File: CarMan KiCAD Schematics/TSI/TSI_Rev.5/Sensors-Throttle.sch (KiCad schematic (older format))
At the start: 55 parts, among them J24 MC+ Short Pin 1, J25 MC+ Short Pin 2, J26 HV+ Short Pin 1, J27 HV+ Short Pin 2, J28 HV- Short Pin 1, J29 HV- Short Pin 2, U21 MCP6004, U25 NCD9830DBR2G, U26 MCP6004, U4 ACPL-C870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

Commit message: Small Changes & Updated PCB
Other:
- moved on the sheet: R104
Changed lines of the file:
@@
 Wire Wire Line
 	11800 5700 11800 5900
-Text Label 10400 5750 0    50   ~ 0
-DiffAmp_REF
-Wire Wire Line
-	10400 5750 10400 5800
 Wire Wire Line
 	10400 6200 10550 6200
@@
 Wire Wire Line
 	13850 4600 13900 4600
-Text Label 14400 4600 0    50   ~ 0
+Text Label 14650 4600 2    50   ~ 0
 MC+
 $Comp
@@
 Wire Wire Line
 	13850 5500 13900 5500
-Text Label 14450 5500 0    50   ~ 0
+Text Label 14650 5500 2    50   ~ 0
 HV+
 $Comp
@@
 Wire Wire Line
 	13850 6300 13900 6300
-Text Label 14400 6300 0    50   ~ 0
+Text Label 14650 6300 2    50   ~ 0
 HV-
 $Comp
@@
 Wire Wire Line
 	12100 4100 12450 4100
-$Comp
-L pspice:CAP C?
-U 1 1 5FA28067
-P 12450 4350
-AR Path="/5FC85F57/5FA28067" Ref="C?"  Part="1"
-AR Path="/6196BF15/5FA28067" Ref="C?"  Part="1"
-AR Path="/5F98EBE9/5FA28067" Ref="C4"  Part="1"
-F 0 "C4" H 12350 4200 50  0000 C CNN
-F 1 "100p" H 12350 4500 50  0000 C CNN
-F 2 "Capacitor_SMD:C_0805_2012Metric_Pad1.15x1.40mm_HandSolder" H 12450 4350 50  0001 C CNN
-F 3 "~" H 12450 4350 50  0001 C CNN
-	1    12450 4350
-	-1   0    0    1
-$EndComp
-Text Label 12100 4050 0    50   ~ 0
-DiffAmp_REF
 $Comp
 L Device:R R53
@@
 	-1   0    0    1
 $EndComp
-Text Label 12100 4950 0    50   ~ 0
-DiffAmp_REF
 Connection ~ 12450 5500
 Wire Wire Line
@@
 	12100 5400 12100 5500
 Wire Wire Line
-	12100 5000 12100 4950
-Connection ~ 12100 5000
-Wire Wire Line
 	11800 4600 12100 4600
-Connection ~ 12450 4600
-Wire Wire Line
-	12450 4600 12800 4600
 Wire Wire Line
 	12100 4500 12100 4600
 Connection ~ 12100 4600
-Wire Wire Line
-	12100 4600 12450 4600
-Wire Wire Line
-	12100 4100 12100 4050
-Connection ~ 12100 4100
 $Comp
 L Device:R R16
@@
 	-1   0    0    1
 $EndComp
-Text Label 12100 5750 0    50   ~ 0
-DiffAmp_REF
 Wire Wire Line
 	12100 6200 12100 6300
-Wire Wire Line
-	12100 5800 12100 5750
-Connection ~ 12100 5800
 Connection ~ 12450 6300
 Wire Wire Line
@@
 Connection ~ 9550 5100
 Wire Wire Line
-	14250 4600 14600 4600
-Wire Wire Line
 	14250 5500 14650 5500
-Wire Wire Line
-	14650 5600 14600 5600
-Wire Wire Line
-	14600 5600 14600 6300
-Wire Wire Line
-	14250 6300 14600 6300
-Wire Wire Line
-	14600 4600 14600 5400
-Wire Wire Line
-	14600 5400 14650 5400
 $Comp
 L TSI_Rev.5-rescue:NCD9830DBR2G-CarMan_KiCAD_Library-TSI_Rev.5-rescue U25
@@
 Wire Wire Line
 	10100 5450 10100 5400
-Text Label 10325 4575 0    50   ~ 0
-DiffAmp_REF
-Wire Wire Line
-	10325 4575 10325 4625
+Wire Wire Line
+	10350 4575 10350 4625
 $Comp
 L Device:R R104
 U 1 1 60749BC2
-P 10325 4775
-F 0 "R104" V 10400 4775 50  0000 C CNN
-F 1 "10K" V 10325 4775 50  0000 C CNN
-F 2 "Resistor_SMD:R_0805_2012Metric_Pad1.15x1.40mm_HandSolder" V 10255 4775 50  0001 C CNN
-F 3 "~" H 10325 4775 50  0001 C CNN
-	1    10325 4775
-	1    0    0    -1
-$EndComp
-Text Label 11125 3450 0    50   ~ 0
-DiffAmp_REF
-Text Label 12225 3450 2    50   ~ 0
+P 10350 4775
+F 0 "R104" V 10425 4775 50  0000 C CNN
+F 1 "10K" V 10350 4775 50  0000 C CNN
+F 2 "Resistor_SMD:R_0805_2012Metric_Pad1.15x1.40mm_HandSolder" V 10280 4775 50  0001 C CNN
+F 3 "~" H 10350 4775 50  0001 C CNN
+	1    10350 4775
+	1    0    0    -1
+$EndComp
+Wire Wire Line
+	10350 5000 10350 4925
+Connection ~ 10350 5000
+Wire Wire Line
+	10350 5000 10400 5000
+Wire Wire Line
+	10300 5000 10350 5000
+Text Label 10800 4575 2    50   ~ 0
 1.24HV_REF
 Wire Wire Line
-	11125 3450 12225 3450
-Wire Wire Line
-	10300 5000 10325 5000
-Wire Wire Line
-	10325 5000 10325 4925
-Connection ~ 10325 5000
-Wire Wire Line
-	10325 5000 10400 5000
+	10350 4575 10800 4575
+Wire Wire Line
+	10400 5750 10400 5800
+Text Label 10850 5750 2    50   ~ 0
+1.24HV_REF
+Wire Wire Line
+	10400 5750 10850 5750
+Text Label 12100 4100 0    43   ~ 0
+1.24HV_REF
+Wire Wire Line
+	12100 4600 12450 4600
+Wire Wire Line
+	12450 4600 12800 4600
+Connection ~ 12450 4600
+$Comp
+L pspice:CAP C?
+U 1 1 5FA28067
+P 12450 4350
+AR Path="/5FC85F57/5FA28067" Ref="C?"  Part="1"
+AR Path="/6196BF15/5FA28067" Ref="C?"  Part="1"
+AR Path="/5F98EBE9/5FA28067" Ref="C4"  Part="1"
+F 0 "C4" H 12350 4200 50  0000 C CNN
+F 1 "100p" H 12350 4500 50  0000 C CNN
+F 2 "Capacitor_SMD:C_0805_2012Metric_Pad1.15x1.40mm_HandSolder" H 12450 4350 50  0001 C CNN
+F 3 "~" H 12450 4350 50  0001 C CNN
+	1    12450 4350
+	-1   0    0    1
+$EndComp
+Text Label 12100 5000 0    43   ~ 0
+1.24HV_REF
+Text Label 12100 5800 0    43   ~ 0
+1.24HV_REF
+Wire Wire Line
+	14250 6300 14650 6300
+Wire Wire Line
+	14250 4600 14650 4600
 $EndSCHEMATC

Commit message: General numbering
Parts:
- renumbered C48 to C39, C47 to C40, C46 to C41, C43 to C42
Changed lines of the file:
@@
 AR Path="/5FC85F57/5FA3E628" Ref="C?"  Part="1"
 AR Path="/6196BF15/5FA3E628" Ref="C?"  Part="1"
-AR Path="/5F98EBE9/5FA3E628" Ref="C48"  Part="1"
-F 0 "C48" H 12350 5100 50  0000 C CNN
+AR Path="/5F98EBE9/5FA3E628" Ref="C39"  Part="1"
+F 0 "C39" H 12350 5100 50  0000 C CNN
 F 1 "100p" H 12350 5400 50  0000 C CNN
 F 2 "Capacitor_SMD:C_0805_2012Metric_Pad1.15x1.40mm_HandSolder" H 12450 5250 50  0001 C CNN
@@
 AR Path="/5FC85F57/5FD6895A" Ref="C?"  Part="1"
 AR Path="/6196BF15/5FD6895A" Ref="C?"  Part="1"
-AR Path="/5F98EBE9/5FD6895A" Ref="C47"  Part="1"
-F 0 "C47" V 6350 3050 50  0000 C CNN
+AR Path="/5F98EBE9/5FD6895A" Ref="C40"  Part="1"
+F 0 "C40" V 6350 3050 50  0000 C CNN
 F 1 "100p" V 6350 2750 50  0000 C CNN
 F 2 "Capacitor_SMD:C_0805_2012Metric_Pad1.15x1.40mm_HandSolder" H 6300 2900 50  0001 C CNN
@@
 AR Path="/5FC85F57/5F9BBB2D" Ref="C?"  Part="1"
 AR Path="/6196BF15/5F9BBB2D" Ref="C?"  Part="1"
-AR Path="/5F98EBE9/5F9BBB2D" Ref="C46"  Part="1"
-F 0 "C46" H 5550 1800 50  0000 C CNN
+AR Path="/5F98EBE9/5F9BBB2D" Ref="C41"  Part="1"
+F 0 "C41" H 5550 1800 50  0000 C CNN
 F 1 "100p" H 5550 1600 50  0000 C CNN
 F 2 "Capacitor_SMD:C_0805_2012Metric_Pad1.15x1.40mm_HandSolder" H 5450 1700 50  0001 C CNN
@@
 AR Path="/5FC85F57/5FA6EAF2" Ref="C?"  Part="1"
 AR Path="/6196BF15/5FA6EAF2" Ref="C?"  Part="1"
-AR Path="/5F98EBE9/5FA6EAF2" Ref="C43"  Part="1"
-F 0 "C43" H 8000 1800 50  0000 C CNN
+AR Path="/5F98EBE9/5FA6EAF2" Ref="C42"  Part="1"
+F 0 "C42" H 8000 1800 50  0000 C CNN
 F 1 "0.1u" H 8000 1600 50  0000 C CNN
 F 2 "Capacitor_SMD:C_0805_2012Metric_Pad1.15x1.40mm_HandSolder" H 7900 1700 50  0001 C CNN

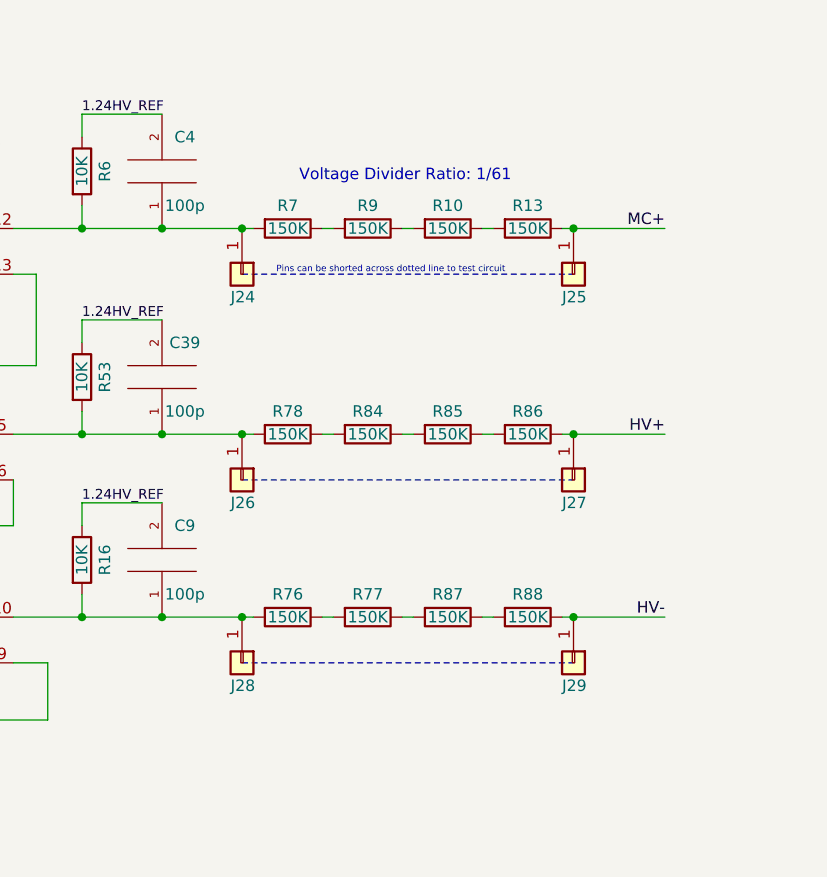
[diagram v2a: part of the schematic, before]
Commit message: Added jumpers across HV-, HV+ & MC+ voltage dividers Comments added to PC Circuit
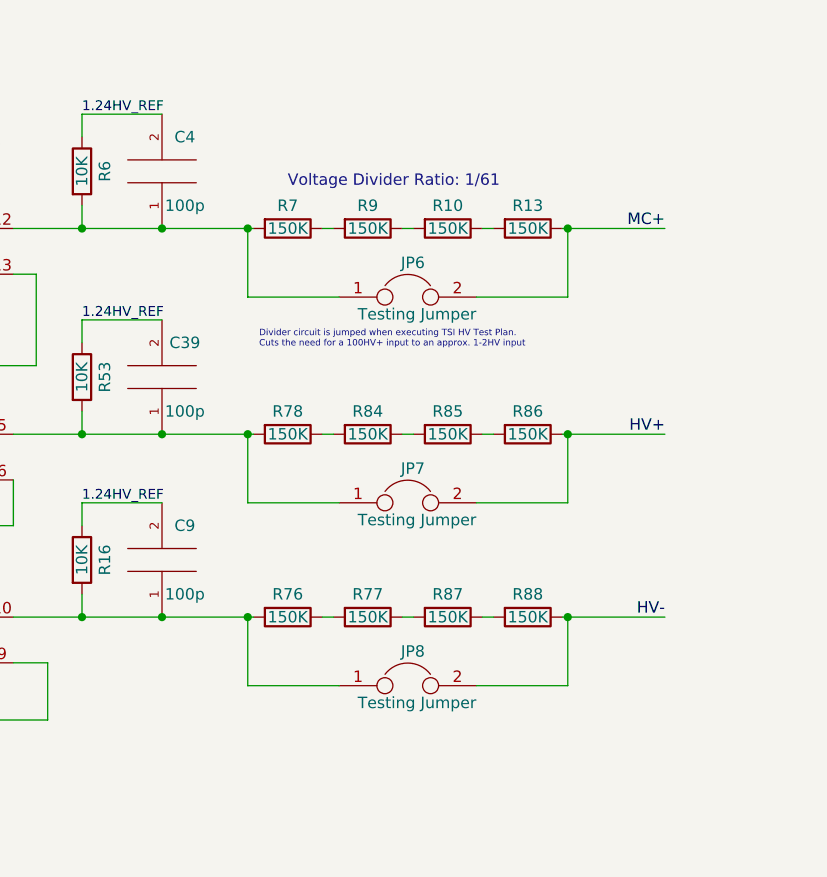
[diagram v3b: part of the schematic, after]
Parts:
- removed J24: MC+ Short Pin 1, Connector_PinSocket_2.54mm:PinSocket_1x01_P2.54mm_Vertical, symbol Connector_Generic:Conn_01x01
- removed J25: MC+ Short Pin 2, Connector_PinSocket_2.54mm:PinSocket_1x01_P2.54mm_Vertical, symbol Connector_Generic:Conn_01x01
- removed J26: HV+ Short Pin 1, Connector_PinSocket_2.54mm:PinSocket_1x01_P2.54mm_Vertical, symbol Connector_Generic:Conn_01x01
- removed J27: HV+ Short Pin 2, Connector_PinSocket_2.54mm:PinSocket_1x01_P2.54mm_Vertical, symbol Connector_Generic:Conn_01x01
- removed J28: HV- Short Pin 1, Connector_PinSocket_2.54mm:PinSocket_1x01_P2.54mm_Vertical, symbol Connector_Generic:Conn_01x01
- removed J29: HV- Short Pin 2, Connector_PinSocket_2.54mm:PinSocket_1x01_P2.54mm_Vertical, symbol Connector_Generic:Conn_01x01
- added JP6, JP7, JP8: Testing Jumper, Connector_PinHeader_2.54mm:PinHeader_1x02_P2.54mm_Vertical, symbol Device:Jumper
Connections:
- net HV+: now also JP7.2
- net HV-: now also JP8.2
- net MC+: now also JP6.2
- net at C39.1, R53.2, R78.2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: now also JP7.1
- net at C9.1, R16.2, R76.2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: now also JP8.1
- net at C4.1, R6.2, R7.2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: now also JP6.1
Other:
- note added: "Divider circuit is jumped when executing TSI HV Test Plan.\nCuts the need for a 100HV+ input to an approx. 1-2HV input"
- note removed: "Pins can be shorted across dotted line to test circuit"
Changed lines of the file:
@@
 HV-
-$Comp
-L Connector_Generic:Conn_01x01 J27
-U 1 1 5FA0FD5E
-P 14250 5700
-F 0 "J27" V 14350 5650 50  0000 L CNN
-F 1 "HV+ Short Pin 2" V 14350 5500 50  0001 L CNN
-F 2 "Connector_PinSocket_2.54mm:PinSocket_1x01_P2.54mm_Vertical" H 14250 5700 50  0001 C CNN
-F 3 "~" H 14250 5700 50  0001 C CNN
-	1    14250 5700
-	0    1    1    0
-$EndComp
-Connection ~ 14250 5500
-Wire Wire Line
-	14250 5500 14200 5500
-$Comp
-L Connector_Generic:Conn_01x01 J25
-U 1 1 5FA1321C
-P 14250 4800
-F 0 "J25" V 14350 4750 50  0000 L CNN
-F 1 "MC+ Short Pin 2" V 14213 4880 50  0001 L CNN
-F 2 "Connector_PinSocket_2.54mm:PinSocket_1x01_P2.54mm_Vertical" H 14250 4800 50  0001 C CNN
-F 3 "~" H 14250 4800 50  0001 C CNN
-	1    14250 4800
-	0    1    1    0
-$EndComp
-Connection ~ 14250 4600
-Wire Wire Line
-	14250 4600 14200 4600
-Connection ~ 14250 6300
-Wire Wire Line
-	14250 6300 14200 6300
-$Comp
-L Connector_Generic:Conn_01x01 J29
-U 1 1 5FA159E3
-P 14250 6500
-F 0 "J29" V 14350 6450 50  0000 L CNN
-F 1 "HV- Short Pin 2" V 14350 6300 50  0001 L CNN
-F 2 "Connector_PinSocket_2.54mm:PinSocket_1x01_P2.54mm_Vertical" H 14250 6500 50  0001 C CNN
-F 3 "~" H 14250 6500 50  0001 C CNN
-	1    14250 6500
-	0    1    1    0
-$EndComp
-$Comp
-L Connector_Generic:Conn_01x01 J28
-U 1 1 5FA19A24
-P 12800 6500
-F 0 "J28" V 12900 6450 50  0000 L CNN
-F 1 "HV- Short Pin 1" V 12900 6300 50  0001 L CNN
-F 2 "Connector_PinSocket_2.54mm:PinSocket_1x01_P2.54mm_Vertical" H 12800 6500 50  0001 C CNN
-F 3 "~" H 12800 6500 50  0001 C CNN
-	1    12800 6500
-	0    1    1    0
-$EndComp
-Connection ~ 12800 6300
-Wire Wire Line
-	12800 6300 12850 6300
-$Comp
-L Connector_Generic:Conn_01x01 J26
-U 1 1 5FA1EF37
-P 12800 5700
-F 0 "J26" V 12900 5650 50  0000 L CNN
-F 1 "HV+ Short Pin 1" V 12900 5500 50  0001 L CNN
-F 2 "Connector_PinSocket_2.54mm:PinSocket_1x01_P2.54mm_Vertical" H 12800 5700 50  0001 C CNN
-F 3 "~" H 12800 5700 50  0001 C CNN
-	1    12800 5700
-	0    1    1    0
-$EndComp
-Connection ~ 12800 5500
-Wire Wire Line
-	12800 5500 12850 5500
-$Comp
-L Connector_Generic:Conn_01x01 J24
-U 1 1 5FA20DB0
-P 12800 4800
-F 0 "J24" V 12900 4750 50  0000 L CNN
-F 1 "MC+ Short Pin 1" V 12900 4600 50  0001 L CNN
-F 2 "Connector_PinSocket_2.54mm:PinSocket_1x01_P2.54mm_Vertical" H 12800 4800 50  0001 C CNN
-F 3 "~" H 12800 4800 50  0001 C CNN
-	1    12800 4800
-	0    1    1    0
-$EndComp
-Connection ~ 12800 4600
-Wire Wire Line
-	12800 4600 12850 4600
 $Comp
 L Device:R R6
@@
 $EndComp
 Connection ~ 12450 5500
-Wire Wire Line
-	12450 5500 12800 5500
 Connection ~ 12100 5500
 Wire Wire Line
@@
 	12100 6200 12100 6300
 Connection ~ 12450 6300
-Wire Wire Line
-	12450 6300 12800 6300
 Connection ~ 12100 6300
 Wire Wire Line
 	12100 6300 12450 6300
-Wire Notes Line
-	12800 6500 14250 6500
-Wire Notes Line
-	12800 5700 14250 5700
-Wire Notes Line
-	12800 4800 14250 4800
-Text Notes 12950 4800 0    28   ~ 0
-Pins can be shorted across dotted line to test circuit
-Text Notes 13050 4400 0    50   ~ 0
+Text Notes 12875 5125 0    28   ~ 0
+Divider circuit is jumped when executing TSI HV Test Plan.\nCuts the need for a 100HV+ input to an approx. 1-2HV input
+Text Notes 13000 4425 0    50   ~ 0
 Voltage Divider Ratio: 1/61
 Connection ~ 9550 6300
@@
 Difference between \nMC+ & HV-
 Connection ~ 9550 5100
-Wire Wire Line
-	14250 5500 14650 5500
 $Comp
 L TSI_Rev.5-rescue:NCD9830DBR2G-CarMan_KiCAD_Library-TSI_Rev.5-rescue U25
@@
 Wire Wire Line
 	12100 4600 12450 4600
-Wire Wire Line
-	12450 4600 12800 4600
 Connection ~ 12450 4600
 $Comp
@@
 Text Label 12100 5800 0    43   ~ 0
 1.24HV_REF
-Wire Wire Line
-	14250 6300 14650 6300
-Wire Wire Line
-	14250 4600 14650 4600
+$Comp
+L Device:Jumper JP?
+U 1 1 60DE9F20
+P 13525 6600
+AR Path="/6196BF15/60DE9F20" Ref="JP?"  Part="1"
+AR Path="/5F98EBE9/60DE9F20" Ref="JP8"  Part="1"
+F 0 "JP8" H 13600 6750 50  0000 R CNN
+F 1 "Testing Jumper" H 13825 6525 50  0000 R CNN
+F 2 "Connector_PinHeader_2.54mm:PinHeader_1x02_P2.54mm_Vertical" H 13525 6600 50  0001 C CNN
+F 3 "~" H 13525 6600 50  0001 C CNN
+	1    13525 6600
+	1    0    0    -1
+$EndComp
+Wire Wire Line
+	12450 6300 12825 6300
+Wire Wire Line
+	13225 6600 12825 6600
+Wire Wire Line
+	12825 6600 12825 6300
+Connection ~ 12825 6300
+Wire Wire Line
+	12825 6300 12850 6300
+Wire Wire Line
+	14200 6300 14225 6300
+Wire Wire Line
+	14225 6300 14225 6600
+Wire Wire Line
+	14225 6600 13825 6600
+Connection ~ 14225 6300
+Wire Wire Line
+	14225 6300 14650 6300
+$Comp
+L Device:Jumper JP?
+U 1 1 60E70E72
+P 13525 5800
+AR Path="/6196BF15/60E70E72" Ref="JP?"  Part="1"
+AR Path="/5F98EBE9/60E70E72" Ref="JP7"  Part="1"
+F 0 "JP7" H 13600 5950 50  0000 R CNN
+F 1 "Testing Jumper" H 13825 5725 50  0000 R CNN
+F 2 "Connector_PinHeader_2.54mm:PinHeader_1x02_P2.54mm_Vertical" H 13525 5800 50  0001 C CNN
+F 3 "~" H 13525 5800 50  0001 C CNN
+	1    13525 5800
+	1    0    0    -1
+$EndComp
+Wire Wire Line
+	13225 5800 12825 5800
+Wire Wire Line
+	14225 5800 13825 5800
+Wire Wire Line
+	14225 5800 14225 5500
+Wire Wire Line
+	14200 5500 14225 5500
+Connection ~ 14225 5500
+Wire Wire Line
+	14225 5500 14650 5500
+Wire Wire Line
+	12825 5800 12825 5500
+Wire Wire Line
+	12450 5500 12825 5500
+Connection ~ 12825 5500
+Wire Wire Line
+	12825 5500 12850 5500
+Wire Wire Line
+	14200 4600 14225 4600
+Wire Wire Line
+	12450 4600 12825 4600
+$Comp
+L Device:Jumper JP?
+U 1 1 60EC5BB0
+P 13525 4900
+AR Path="/6196BF15/60EC5BB0" Ref="JP?"  Part="1"
+AR Path="/5F98EBE9/60EC5BB0" Ref="JP6"  Part="1"
+F 0 "JP6" H 13600 5050 50  0000 R CNN
+F 1 "Testing Jumper" H 13825 4825 50  0000 R CNN
+F 2 "Connector_PinHeader_2.54mm:PinHeader_1x02_P2.54mm_Vertical" H 13525 4900 50  0001 C CNN
+F 3 "~" H 13525 4900 50  0001 C CNN
+	1    13525 4900
+	1    0    0    -1
+$EndComp
+Wire Wire Line
+	13225 4900 12825 4900
+Wire Wire Line
+	14225 4900 13825 4900
+Wire Wire Line
+	14225 4900 14225 4600
+Connection ~ 14225 4600
+Wire Wire Line
+	14225 4600 14650 4600
+Wire Wire Line
+	12825 4900 12825 4600
+Connection ~ 12825 4600
+Wire Wire Line
+	12825 4600 12850 4600
 $EndSCHEMATC

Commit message: Updated Resistor values for LEDs
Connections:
- net TSV_Voltage renamed TS_Voltage
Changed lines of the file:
@@
 MC_Voltage
 Text Label 8200 5250 0    50   ~ 0
-TSV_Voltage
+TS_Voltage
 Text Label 5750 5400 2    50   ~ 0
 SDA_HV
@@
 HV+
 Text Label 6400 8900 2    50   ~ 0
-TSV_Voltage
+TS_Voltage
 Text Label 6400 9100 2    50   ~ 0
 MC+
 Text HLabel 5750 8900 0    50   Input ~ 0
-TSV_Voltage
+TS_Voltage
 Text HLabel 5750 9100 0    50   Input ~ 0
 MC+

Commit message: Added back 1.24HV_Ref signal. One reference signal purely supplies 1.24HV pull up for Sensors_Throttle_Voltage sheet. The other reference, which is adjustable by potentiometer RV3, drives the TSV_MIN_REF signal. Explanations and notes added
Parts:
- added IC2: TS431ILT, TSI_Rev_2021_Footprint_Lib:SOT95P280X145-5N, symbol CarMan_KiCAD_Library:TS431ILT
- added R70: 1K, Resistor_SMD:R_0805_2012Metric_Pad1.15x1.40mm_HandSolder, symbol Device:R
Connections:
- wire segments 197 -> 205
- no-connect marks 4 -> 6
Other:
- note added: "1.24HV Diff-Amp Reference\n\n\n"
- note added: "VOLTAGE REFERNCE"
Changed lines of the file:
@@
 Text HLabel 2100 9150 0    50   Input ~ 0
 Throttle_LV
-Text HLabel 5750 9700 0    50   Input ~ 0
-1.24HV_REF
 Text HLabel 5750 8800 0    50   Input ~ 0
 IO_Ground
@@
 Text Label 6400 9400 2    50   ~ 0
 Throttle_HV
-Text Label 6400 9700 2    50   ~ 0
-1.24HV_REF
 Text Label 6400 8700 2    50   ~ 0
 5HV
@@
 Text HLabel 5750 9600 0    50   Input ~ 0
 A2_HV
-Wire Notes Line
-	5050 9850 6650 9850
-Wire Notes Line
-	5050 8350 6650 8350
 $Comp
 L Amplifier_Operational:MCP6004 U26
@@
 Wire Wire Line
 	6550 5250 6850 5250
-Wire Notes Line
-	6650 8350 6650 9850
-Wire Notes Line
-	5050 8350 5050 9850
 Wire Wire Line
 	5750 8900 6400 8900
@@
 Wire Wire Line
 	5750 9600 6400 9600
-Wire Wire Line
-	5750 9700 6400 9700
 Wire Notes Line
 	2950 9250 2950 8350
@@
 Wire Wire Line
 	12825 4600 12850 4600
+Wire Wire Line
+	13650 8600 13650 9200
+Wire Wire Line
+	13650 9200 13950 9200
+Wire Wire Line
+	13650 8450 13650 8600
+Connection ~ 13650 8600
+Text Label 13750 8600 0    47   ~ 0
+1.24HV_REF
+$Comp
+L Device:R R?
+U 1 1 6082F46E
+P 13400 9200
+AR Path="/6196BF15/6082F46E" Ref="R?"  Part="1"
+AR Path="/5F98EBE9/6082F46E" Ref="R70"  Part="1"
+F 0 "R70" V 13500 9100 50  0000 L CNN
+F 1 "1K" V 13400 9150 50  0000 L CNN
+F 2 "Resistor_SMD:R_0805_2012Metric_Pad1.15x1.40mm_HandSolder" V 13330 9200 50  0001 C CNN
+F 3 "~" H 13400 9200 50  0001 C CNN
+	1    13400 9200
+	0    -1   -1   0
+$EndComp
+Wire Wire Line
+	13550 9200 13650 9200
+Connection ~ 13650 9200
+Text Label 12950 9200 0    59   ~ 0
+5HV
+Text Label 15050 9000 2    47   ~ 0
+IO_Ground
+NoConn ~ 13950 9000
+NoConn ~ 13950 9100
+Text Notes 13525 9850 0    59   ~ 0
+1.24HV Diff-Amp Reference\n\n\n
+$Comp
+L CarMan_KiCAD_Library:TS431ILT IC?
+U 1 1 6082F485
+P 14300 9100
+AR Path="/6196BF15/6082F485" Ref="IC?"  Part="1"
+AR Path="/5F98EBE9/6082F485" Ref="IC2"  Part="1"
+F 0 "IC2" H 14300 9400 79  0000 C CNN
+F 1 "TS431ILT" H 14300 8800 79  0000 C CNN
+F 2 "TSI_Rev_2021_Footprint_Lib:SOT95P280X145-5N" H 14050 9200 79  0001 C CNN
+F 3 "https://www.snapeda.com/parts/TS431ILT/STMicroelectronics/datasheet/" H 14050 9200 79  0001 C CNN
+	1    14300 9100
+	1    0    0    -1
+$EndComp
+Wire Wire Line
+	12950 9200 13250 9200
+Wire Wire Line
+	14650 9200 15200 9200
+Wire Wire Line
+	15050 9000 14650 9000
+Wire Wire Line
+	15200 8600 15200 9200
+Wire Wire Line
+	13650 8600 15200 8600
+$Comp
+L power:PWR_FLAG #FLG02
+U 1 1 608F2DD5
+P 13650 8450
+F 0 "#FLG02" H 13650 8525 50  0001 C CNN
+F 1 "PWR_FLAG" H 13650 8623 50  0000 C CNN
+F 2 "" H 13650 8450 50  0001 C CNN
+F 3 "~" H 13650 8450 50  0001 C CNN
+	1    13650 8450
+	1    0    0    -1
+$EndComp
+Wire Notes Line
+	5050 9700 6650 9700
+Wire Notes Line
+	6650 9700 6650 8350
+Wire Notes Line
+	5050 9700 5050 8350
+Wire Notes Line
+	5050 8350 6650 8350
+Wire Notes Line
+	12750 9700 15400 9700
+Text Notes 13550 8000 0    79   ~ 0
+VOLTAGE REFERNCE
+Wire Notes Line
+	15400 7850 15400 9700
+Wire Notes Line
+	12750 7850 15400 7850
+Wire Notes Line
+	12750 7850 12750 9700
 $EndSCHEMATC
